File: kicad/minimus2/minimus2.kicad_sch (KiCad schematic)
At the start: 71 parts, among them P3 CONN_1, P4 CONN_1, P5 CONN_1, P6 CONN_1, P7 CHRG&USART, P8 BATT, P9 Actuator, Q5 IRLML6344TRPBFTR, Q6 IRLML6344TRPBFTR, Q7 IRLML6344TRPBFTR, Q8 IRLML6344TRPBFTR, SW2 KMR211GLFS, SW3 SS12D01G4, U10 ENCODER_CONNECT_PCB, U11 LP5907, U3 ENCODER_CONNECT_IC, U6 ENCODER_CONNECT_IC, U7 DRV8836, U8 STM32F411CEU6/STM32F413CHU6, U9 ENCODER_CONNECT_PCB

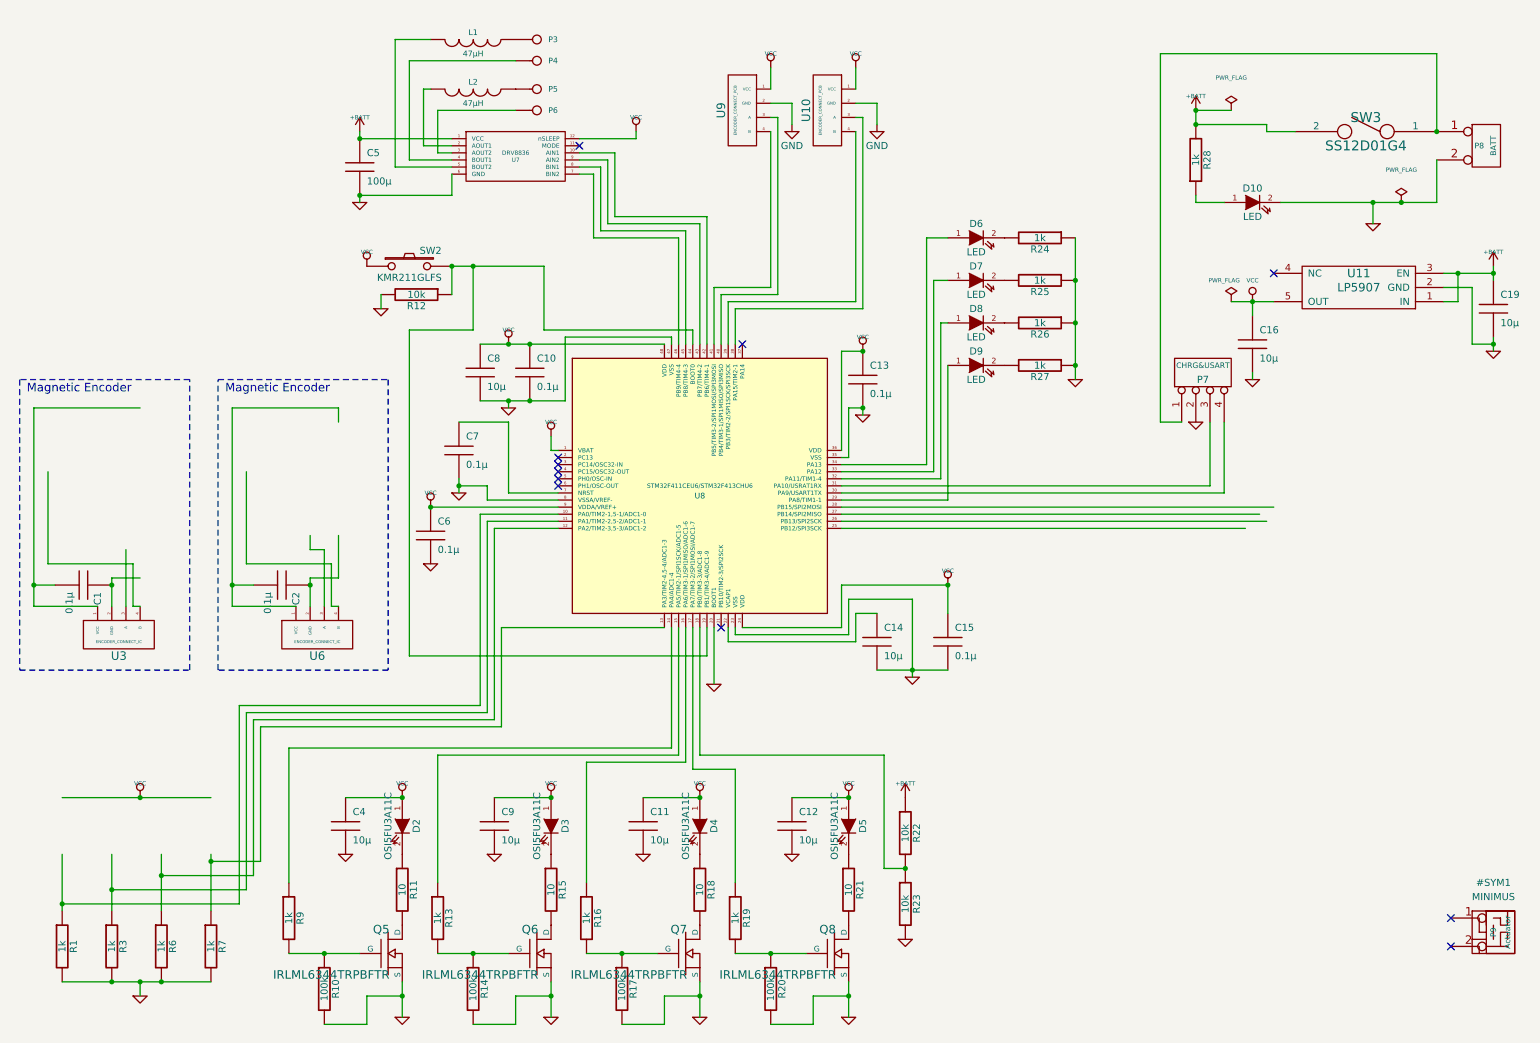
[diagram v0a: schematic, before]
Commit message: start adding parts to schematic
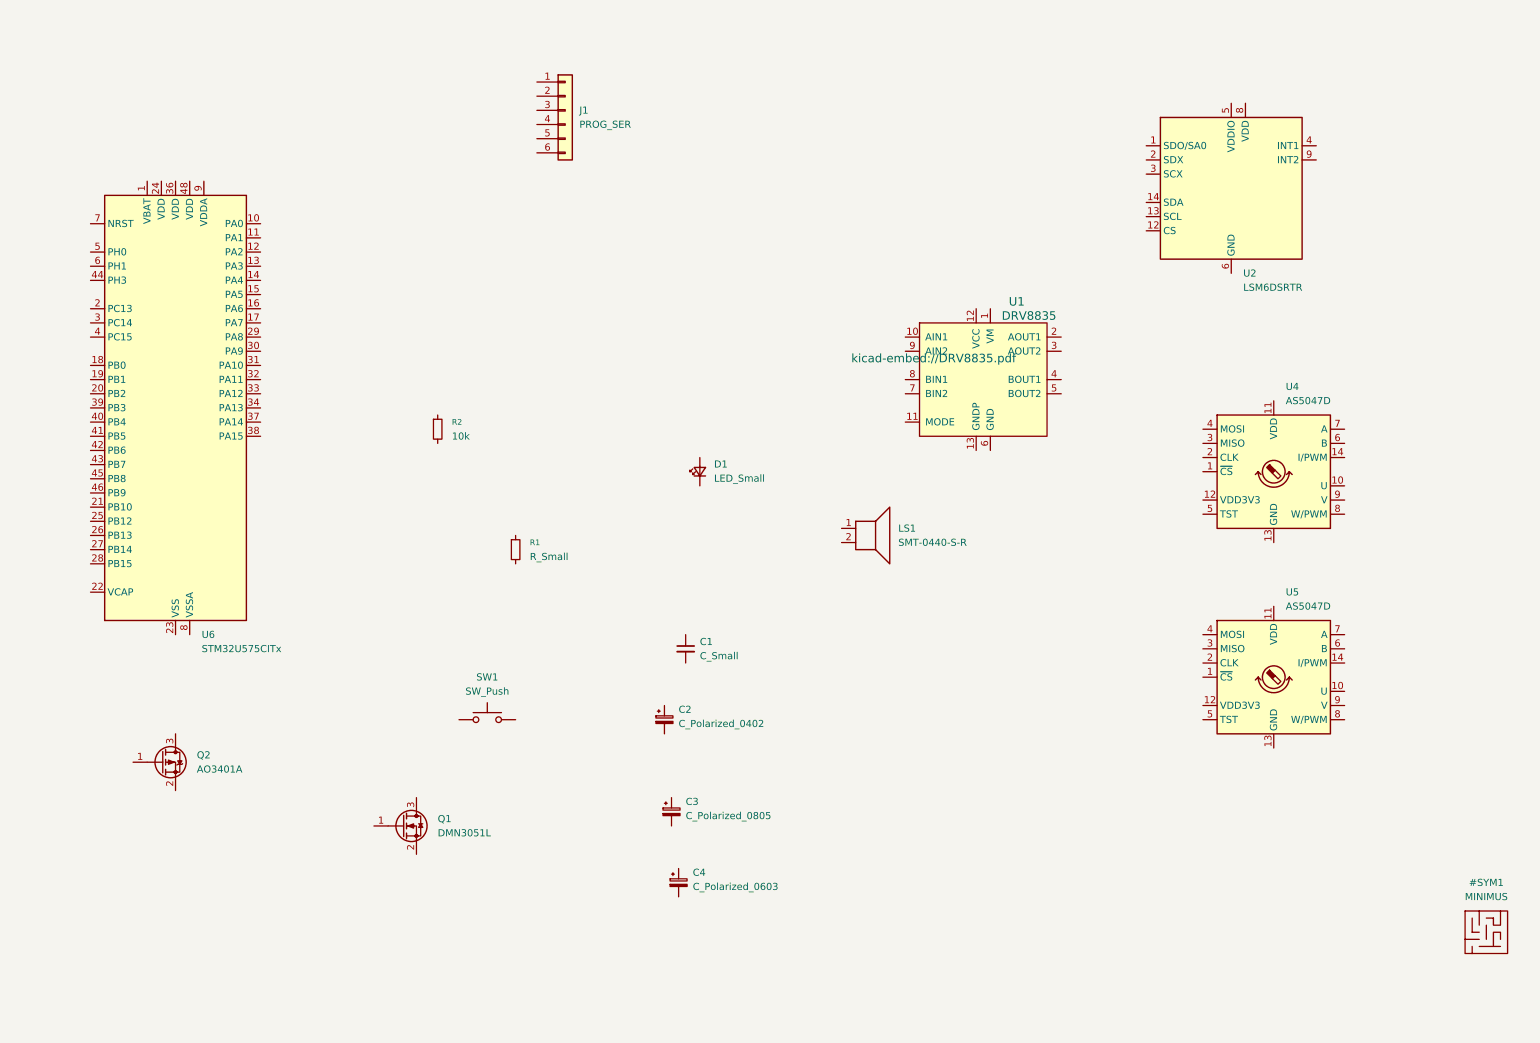
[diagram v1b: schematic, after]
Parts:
- removed C1, C10, C13, C15, C2, C6, C7: 0.1μ, Zirconia:chip1608, symbol Zirconia-rescue:C-RESCUE-Fantom
- removed C11, C12, C14, C16, C19, C4, C8, C9: 10μ, Zirconia:chip1608, symbol Zirconia-rescue:C-RESCUE-Fantom
- removed C5: 100μ, Zirconia:chip3216, symbol Zirconia-rescue:C-RESCUE-Fantom
- removed D10, D6, D7, D8, D9: LED, Zirconia:chip1608, symbol Zirconia-rescue:LED-RESCUE-Fantom
- removed D2, D3, D4, D5: OSI5FU3A11C, Zirconia:OSI5FU3A11C, symbol Zirconia-rescue:LED-RESCUE-Fantom
- removed L1, L2: 47μH, Zirconia:Inductor, symbol Zirconia-rescue:INDUCTOR
- removed P3, P4, P5, P6: CONN_1, Zirconia:motor_pin, symbol Zirconia-rescue:CONN_1
- removed P7: CHRG&USART, Zirconia:SH_4pin, symbol Zirconia-rescue:CONN_4
- removed P8: BATT, Zirconia:1.5mm_pin2, symbol Zirconia-rescue:CONN_2
- removed P9: Actuator, Zirconia:Mot_mount, symbol Zirconia-rescue:CONN_2
- removed Q5, Q6, Q7, Q8: IRLML6344TRPBFTR, Zirconia:IRLML6344TRPbF, symbol Zirconia-rescue:MOSFET_N
- removed R1, R13, R16, R19, R24, R25, R26, R27, R28, R3, R6, R7, R9: 1k, Zirconia:chip1608, symbol Zirconia-rescue:R-RESCUE-Fantom
- removed R10, R14, R17, R20: 100k, Zirconia:chip1608, symbol Zirconia-rescue:R-RESCUE-Fantom
- removed R11, R15, R18, R21: 10, Zirconia:chip1608, symbol Zirconia-rescue:R-RESCUE-Fantom
- removed R12, R22, R23: 10k, Zirconia:chip1608, symbol Zirconia-rescue:R-RESCUE-Fantom
- removed SW2: KMR211GLFS, Zirconia:KMR211G, symbol Zirconia-rescue:SW_PUSH
- removed SW3: SS12D01G4, Zirconia:SS12D01G4, symbol Zirconia-rescue:SPST
- removed U10, U9: ENCODER_CONNECT_PCB, Zirconia:ENC_CONN_FLAT, symbol Zirconia-rescue:ENCODER_CONNECT_PCB
- removed U11: LP5907, Zirconia:SOT23, symbol Zirconia-rescue:LP5907
- removed U3, U6: ENCODER_CONNECT_IC, Zirconia:ENC_CONN_VART, symbol Zirconia-rescue:ENCODER_CONNECT_IC
- removed U7: DRV8836, Zirconia:DRV8836, symbol Zirconia-rescue:DRV8836
- removed U8: STM32F411CEU6/STM32F413CHU6, Package_QFP:TQFP-48_7x7mm_P0.5mm, symbol Zirconia-rescue:STM32F411CEU6
- added C1: C_Small, Capacitor_SMD:C_0402_1005Metric, symbol Device:C_Small
- added C2: C_Polarized_0402, Capacitor_SMD:C_0402_1005Metric, symbol Device:C_Polarized_Small
- added C3: C_Polarized_0805, Capacitor_SMD:C_0805_2012Metric, symbol Device:C_Polarized_Small
- added C4: C_Polarized_0603, Capacitor_SMD:C_0603_1608Metric, symbol Device:C_Polarized_Small
- added D1: LED_Small, LED_SMD:LED_0402_1005Metric, symbol Device:LED_Small
- added J1: PROG_SER, Connector_JST:JST_SH_BM06B-SRSS-TB_1x06-1MP_P1.00mm_Vertical, symbol Connector_Generic:Conn_01x06
- added LS1: SMT-0440-S-R, minimus:SMT-0440-S-R, symbol Device:Speaker
- added Q1: DMN3051L, Package_TO_SOT_SMD:SOT-23, symbol Transistor_FET:DMN3051L
- added Q2: AO3401A, Package_TO_SOT_SMD:SOT-23, symbol Transistor_FET:AO3401A
- added R1: R_Small, Resistor_SMD:R_0402_1005Metric, symbol Device:R_Small
- added R2: 10k, Resistor_SMD:R_0402_1005Metric, symbol Device:R_Small
- added SW1: SW_Push, minimus:EVPBB, symbol minimus:SW_Push
- added U1: DRV8835, Package_SON:WSON-12-1EP_3x2mm_P0.5mm_EP1x2.65_ThermalVias, symbol minimus:DRV8835
- added U2: LSM6DSRTR, Package_LGA:LGA-14_3x2.5mm_P0.5mm_LayoutBorder3x4y, symbol Sensor_Motion:LSM6DS3
- added U4, U5: AS5047D, Package_SO:TSSOP-14_4.4x5mm_P0.65mm, symbol Sensor_Magnetic:AS5047D
- added U6: STM32U575CITx, Package_QFP:LQFP-48_7x7mm_P0.5mm, symbol MCU_ST_STM32U5:STM32U575CITx
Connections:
- new net: U6.23 (VSS), U6.35 (VSS), U6.47 (VSS)
- new net: U2.6 (GND), U2.7 (GND)
- no-connect marks 11 -> 0
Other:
- note removed: "Magnetic Encoder"

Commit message: update kiad files
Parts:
- added D2, D3, D4, D5: LED_Small, LED_THT:LED_D3.0mm_Horizontal_O1.27mm_Z2.0mm_IRBlack, symbol Device:LED_Small
- added J4, J6: Conn_01x01, minimus:Motor Red, symbol Connector_Generic:Conn_01x01
- added J5, J7: Conn_01x01, minimus:Motor Blk, symbol Connector_Generic:Conn_01x01
- added L1, L2: 47uH, minimus:IFSC-1515AH-01, symbol Device:L
- added Q3, Q4, Q5, Q6: SFH309, LED_THT:LED_D3.0mm_Horizontal_O1.27mm_Z2.0mm_Clear, symbol Sensor_Optical:SFH309
- added Q7, Q8, Q9: DMN3051L, Package_TO_SOT_SMD:SOT-23, symbol Transistor_FET:DMN3051L
- added SW2: RESET, Button_Switch_SMD:SW_Push_1P1T_NO_CK_KMR2, symbol minimus:SW_Push
- J1: Digikey (none) -> https://www.digikey.jp/short/9jmh9z9j
- LS1: value SMT-0440-S-R -> SMT-0340-T-R; footprint minimus:SMT-0440-S-R -> minimus:SMT-0340-T-R; LCSC (none) -> C3811754
- Q1: LCSC (none) -> C155348
- Q2: LCSC (none) -> C15127
- SW1: value SW_Push -> USER_A; footprint minimus:EVPBB -> Button_Switch_SMD:SW_Push_1P1T_NO_CK_KMR2
- U1: footprint Package_SON:WSON-12-1EP_3x2mm_P0.5mm_EP1x2.65_ThermalVias -> minimus:DRV8835
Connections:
- net GND: now reaches U4.13 (GND)
- net GND: now also U1.13 (GNDP), U1.6 (GND), U2.6 (GND), U2.7 (GND), U5.13 (GND), U6.23 (VSS), U6.35 (VSS), U6.47 (VSS), U6.8 (VSSA), SW2.2
- net +BATT: now reaches U1.1 (VM)
- net L_MOT1: now reaches U1.10 (AIN1)
- net +3.3V: now reaches U1.12 (VCC)
- net at U1.2 (AOUT1): now also L1.1
- net at U1.3 (AOUT2): now also J5.1 (Pin_1)
- net at U1.4 (BOUT1): now also L2.1
- net at U1.5 (BOUT2): now also J7.1 (Pin_1)
- net R_MOT2: now reaches U1.7 (BIN2)
- net R_MOT1: now reaches U1.8 (BIN1)
- net L_MOT2: now reaches U1.9 (AIN2)
- new net: J4.1 (Pin_1), L1.2
- new net: J6.1 (Pin_1), L2.2
- no-connect marks 0 -> 1
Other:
- moved on the sheet: U1, U2, U4

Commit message: Rough place most parts
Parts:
- removed C1: C_Small, Capacitor_SMD:C_0402_1005Metric, symbol Device:C_Small
- removed C2: C_Polarized_0402, Capacitor_SMD:C_0402_1005Metric, symbol Device:C_Polarized_Small
- removed C3: C_Polarized_0805, Capacitor_SMD:C_0805_2012Metric, symbol Device:C_Polarized_Small
- removed C4: C_Polarized_0603, Capacitor_SMD:C_0603_1608Metric, symbol Device:C_Polarized_Small
- removed J4, J6: Conn_01x01, minimus:Motor Red, symbol Connector_Generic:Conn_01x01
- removed J5, J7: Conn_01x01, minimus:Motor Blk, symbol Connector_Generic:Conn_01x01
- removed Q2: AO3401A, Package_TO_SOT_SMD:SOT-23, symbol Transistor_FET:AO3401A
- removed Q4, Q5, Q6: SFH309, LED_THT:LED_D3.0mm_Horizontal_O1.27mm_Z2.0mm_Clear, symbol Sensor_Optical:SFH309
- removed Q7, Q8, Q9: DMN3051L, Package_TO_SOT_SMD:SOT-23, symbol Transistor_FET:DMN3051L
- removed U6: STM32U575CITx, Package_QFP:LQFP-48_7x7mm_P0.5mm, symbol MCU_ST_STM32U5:STM32U575CITx
- added C1, C7: 4.7uF, Capacitor_SMD:C_0805_2012Metric, symbol Device:C_Polarized_Small
- added C2, C3, C4, C5, C6, C8: 100nF, Capacitor_SMD:C_0402_1005Metric, symbol minimus:C_Small
- added D5: LED, LED_SMD:LED_0402_1005Metric, symbol Device:LED_Small
- added J2, J3: LM, Connector_PinHeader_2.00mm:PinHeader_1x02_P2.00mm_Vertical, symbol Connector:Conn_01x02_Socket
- added LFE1, LSE1, RSE1: SFH4050, LED_THT:LED_D3.0mm_Horizontal_O1.27mm_Z2.0mm_IRBlack, symbol Device:LED_Small
- added LSS1, RFS1, RSS1: SFH309, LED_THT:LED_D3.0mm_Horizontal_O1.27mm_Z2.0mm_Clear, symbol Sensor_Optical:SFH309
- added NT1: NetTie_2, NetTie:NetTie-2_SMD_Pad0.5mm, symbol Device:NetTie_2
- added Q1: RSE, Package_TO_SOT_SMD:SOT-23, symbol Transistor_FET:DMN3051L
- added Q3: LFE, Package_TO_SOT_SMD:SOT-23, symbol Transistor_FET:DMN3051L
- added Q4: LSE, Package_TO_SOT_SMD:SOT-23, symbol Transistor_FET:DMN3051L
- added Q5: DMN3051L, Package_TO_SOT_SMD:SOT-23, symbol Transistor_FET:DMN3051L
- added R10, R13, R17, R18, R19, R20, R21, R22, R23, R24, R25, R26, R3, R4, R9: 1k0, Resistor_SMD:R_0402_1005Metric, symbol Device:R_Small
- added R11, R12, R15, R16, R5, R6: 47k, Resistor_SMD:R_0402_1005Metric, symbol Device:R_Small
- added R14: 10k, Resistor_SMD:R_0402_1005Metric, symbol Device:R_Small
- added R7, R8: 33R, Resistor_SMD:R_0402_1005Metric, symbol Device:R_Small
- added SW1: RESET, Button_Switch_SMD:SW_Push_1P1T_NO_CK_KMR2, symbol minimus:SW_Push
- added TP1: BOOT_SEL, TestPoint:TestPoint_Pad_D1.0mm, symbol Connector:TestPoint
- added U2: STM32U575CITx, Package_QFP:LQFP-48_7x7mm_P0.5mm, symbol minimus:STM32U575CITx-FUNC
- D1: value LED_Small -> LED
- D2, D3, D4: value LED_Small -> LED; footprint LED_THT:LED_D3.0mm_Horizontal_O1.27mm_Z2.0mm_IRBlack -> LED_SMD:LED_0402_1005Metric
- J1: footprint Connector_JST:JST_SH_BM06B-SRSS-TB_1x06-1MP_P1.00mm_Vertical -> Connector_PinHeader_1.27mm:PinHeader_2x03_P1.27mm_Vertical
- Q2: renamed from Q1; value DMN3051L -> RFE
- R1: value R_Small -> 33R
- R2: value 10k -> 33R; LCSC C25744 -> (none)
- RFE1: renamed from D5; value LED_Small -> SFH4050
- SW3: renamed from SW2; value RESET -> USER_B
- renumbered Q3 to LFS1, SW1 to SW2, U2 to U1, U1 to U3
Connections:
- net +3.3V: now also LS1.1, SW2.2, SW3.1, C3.1, C4.1, C5.1, C6.1, R14.1, U2.1 (VBAT), U2.24 (VDD), U2.36 (VDD), U2.48 (VDD)
- net GND: now also Q2.2 (S), C3.2, C4.2, C5.2, C6.2, C7.2, C8.2, NT1.1, Q1.2 (S), Q3.2 (S), Q4.2 (S), Q5.2 (S), R11.2, R12.2, R13.2, R15.2, R16.2, R22.2, R23.2, R24.2, R25.2, R26.2, R5.2, R6.2, SW1.1, U2.23 (VSS), U2.35 (VSS), U2.47 (VSS); no longer SW3.2
- net at L1.2: now also J2.1 (Pin_1)
- net SW_A: now reaches SW2.1
- net SW_A: now also R15.1
- net at U3.3 (AOUT2): now also J2.2 (Pin_2)
- net at U3.5 (BOUT2): now also J3.2 (Pin_2)
- net +3.3VA: now reaches LFS1.1 (C)
- net +3.3VA: now also C1.1, C2.1, LSS1.1 (C), RFS1.1 (C), RSS1.1 (C), U2.9 (VDDA)
- net LFS: now reaches LFS1.2 (E)
- net LFS: now also R17.1
- net +5V: now reaches R2.1
- net +5V: now also R1.1, R7.1, R8.1
- net at R2.2: now also RFE1.2 (A)
- net at R1.2: now also RSE1.2 (A)
- net at D1.1 (K): now also R13.1
- net at D1.2 (A): now also TP1.1, U2.44 (PH3/BOOT0)
- net at Q2.1 (G): now also R4.2, R6.1
- net at Q2.3 (D): now also RFE1.1 (K)
- net at L2.2: now also J3.1 (Pin_1)
- net at LS1.2: now also Q5.3 (D)
- net at D3.1 (K): now also R23.1
- net at D4.1 (K): now also R24.1
- net at D2.1 (K): now also R22.1
- new net: LSE1.1 (K), Q4.3 (D)
- new net: LSE1.2 (A), R8.2
- new net: Q3.1 (G), R11.1, R9.2
- new net: LFE1.1 (K), Q3.3 (D)
- new net: C7.1, U2.22 (VCAP)
- new net: Q1.1 (G), R3.2, R5.1
- new net: Q1.3 (D), RSE1.1 (K)
- new net: Q5.1 (G), R21.2, R26.1
- new net: Q4.1 (G), R10.2, R12.1
- new net: D5.1 (K), R25.1
- new net: LFE1.2 (A), R7.2
- new net GNDA: C1.2, C2.2, NT1.2, R17.2, R18.2, R19.2, R20.2, U2.8 (VSSA)
- new net LFE: R9.1
- new net LSE: R10.1
- new net LSS: LSS1.2 (E), R18.1
- new net NRST: C8.1, R14.2, SW1.2
- new net RFE: R4.1
- new net RFS: R20.1, RFS1.2 (E)
- new net RSE: R3.1
- new net RSS: R19.1, RSS1.2 (E)
- new net SPKR: R21.1
- new net SW_B: R16.1, SW3.2
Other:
- moved on the sheet: J1, L1, L2, LFS1, LS1, Q2, RFE1, SW2, SW3, U1, U3, U4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
